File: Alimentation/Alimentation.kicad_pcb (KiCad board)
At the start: 2 copper layers, 63.5 x 108 mm, 18 parts, among them J1 connector_battery, J2 connector_battery, J3 RJ_can, J4 USB_A, J5 Conn_01x02_Male, J6 Conn_01x03_Male, J7 Conn_01x02_Male, U1 JCK2012S12, U2 JCK2012S05

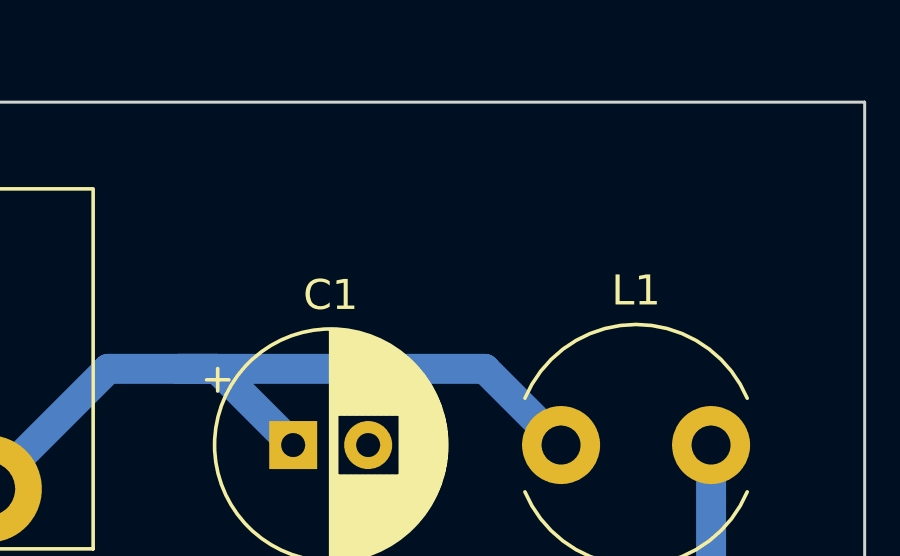
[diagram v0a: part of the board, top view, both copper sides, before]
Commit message: Ajout de la led
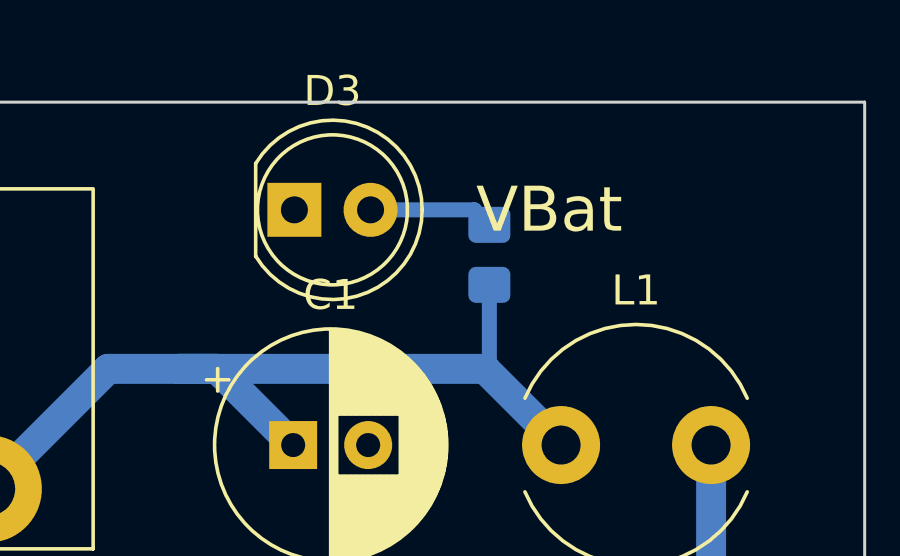
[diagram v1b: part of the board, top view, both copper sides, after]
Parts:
- added D3: LED, LED_THT:LED_D5.0mm, F.Cu at (124.5, 45.5)
- added R4: 1500, Resistor_SMD:R_0805_2012Metric_Pad1.20x1.40mm_HandSolder, B.Cu at (131.0, 47.0)
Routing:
- net Net-(D3-Pad2): track 0.00 -> 4.17 mm
- net V_batt: track 58.4 -> 61.3 mm
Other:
- board text added: "VBat"
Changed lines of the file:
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@@
   (net 15 "unconnected-(U2-Pad4)")
   (net 16 "unconnected-(U2-Pad6)")
+  (net 17 "Net-(D3-Pad2)")
   (footprint "Inductor_THT:L_Radial_D7.8mm_P5.00mm_Fastron_07HCP" (layer "F.Cu")
     (at 133.39 53.34)
@@
     )
   )
+  (footprint "LED_THT:LED_D5.0mm" (layer "F.Cu")
+    (at 124.5 45.5)
+    (descr "LED, diameter 5.0mm, 2 pins, http://cdn-reichelt.de/documents/datenblatt/A500/LL-504BC2E-009.pdf")
+    (tags "LED diameter 5.0mm 2 pins")
+    (property "Sheetfile" "Alimentation.kicad_sch")
+    (property "Sheetname" "")
+    (attr through_hole)
+    (fp_text reference "D3" (at 1.27 -3.96) (layer "F.SilkS")
+      (effects (font (size 1 1) (thickness 0.15)))
+    )
+    (fp_text value "LED" (at 1.27 3.96) (layer "F.Fab")
+      (effects (font (size 1 1) (thickness 0.15)))
+    )
+    (fp_text user "${REFERENCE}" (at 1.25 0) (layer "F.Fab")
+      (effects (font (size 0.8 0.8) (thickness 0.2)))
+    )
+    (fp_line (start -1.29 -1.545) (end -1.29 1.545) (layer "F.SilkS") (width 0.12))
+    (fp_arc (start 4.26 -0.000462) (mid 2.072002 2.880433) (end -1.29 1.54483) (layer "F.SilkS") (width 0.12))
+    (fp_arc (start -1.29 -1.54483) (mid 2.072002 -2.880433) (end 4.26 0.000462) (layer "F.SilkS") (width 0.12))
+    (fp_circle (center 1.27 0) (end 3.77 0) (layer "F.SilkS") (width 0.12) (fill none))
+    (fp_line (start -1.95 3.25) (end 4.5 3.25) (layer "F.CrtYd") (width 0.05))
+    (fp_line (start 4.5 3.25) (end 4.5 -3.25) (layer "F.CrtYd") (width 0.05))
+    (fp_line (start -1.95 -3.25) (end -1.95 3.25) (layer "F.CrtYd") (width 0.05))
+    (fp_line (start 4.5 -3.25) (end -1.95 -3.25) (layer "F.CrtYd") (width 0.05))
+    (fp_line (start -1.23 -1.469694) (end -1.23 1.469694) (layer "F.Fab") (width 0.1))
+    (fp_arc (start -1.23 -1.469694) (mid 4.17 0.000016) (end -1.230016 1.469666) (layer "F.Fab") (width 0.1))
+    (fp_circle (center 1.27 0) (end 3.77 0) (layer "F.Fab") (width 0.1) (fill none))
+    (pad "1" thru_hole rect (at 0 0) (size 1.8 1.8) (drill 0.9) (layers *.Cu *.Mask)
+      (net 2 "GND") (pinfunction "K") (pintype "passive"))
+    (pad "2" thru_hole circle (at 2.54 0) (size 1.8 1.8) (drill 0.9) (layers *.Cu *.Mask)
+      (net 17 "Net-(D3-Pad2)") (pinfunction "A") (pintype "passive"))
+    (model "${KICAD6_3DMODEL_DIR}/LED_THT.3dshapes/LED_D5.0mm.wrl"
+      (offset (xyz 0 0 0))
+      (scale (xyz 1 1 1))
+      (rotate (xyz 0 0 0))
+    )
+  )
   (footprint "Connector_PinHeader_2.54mm:PinHeader_1x03_P2.54mm_Horizontal" (layer "F.Cu")
     (at 92.71 129.525 180)
@@
     )
   )
+  (footprint "Resistor_SMD:R_0805_2012Metric_Pad1.20x1.40mm_HandSolder" (layer "B.Cu")
+    (at 131 47 90)
+    (descr "Resistor SMD 0805 (2012 Metric), square (rectangular) end terminal, IPC_7351 nominal with elongated pad for handsoldering. (Body size source: IPC-SM-782 page 72, https://www.pcb-3d.com/wordpress/wp-content/uploads/ipc-sm-782a_amendment_1_and_2.pdf), generated with kicad-footprint-generator")
+    (tags "resistor handsolder")
+    (property "Sheetfile" "Alimentation.kicad_sch")
+    (property "Sheetname" "")
+    (attr smd)
+    (fp_text reference "R4" (at 0 1.65 90) (layer "B.SilkS")
+      (effects (font (size 1 1) (thickness 0.15)) (justify mirror))
+    )
+    (fp_text value "1500" (at 0 -1.65 90) (layer "B.Fab")
+      (effects (font (size 1 1) (thickness 0.15)) (justify mirror))
+    )
+    (fp_text user "${REFERENCE}" (at 0 0 90) (layer "B.Fab")
+      (effects (font (size 0.5 0.5) (thickness 0.08)) (justify mirror))
+    )
+    (fp_line (start -0.227064 -0.735) (end 0.227064 -0.735) (layer "B.SilkS") (width 0.12))
+    (fp_line (start -0.227064 0.735) (end 0.227064 0.735) (layer "B.SilkS") (width 0.12))
+    (fp_line (start 1.85 -0.95) (end -1.85 -0.95) (layer "B.CrtYd") (width 0.05))
+    (fp_line (start 1.85 0.95) (end 1.85 -0.95) (layer "B.CrtYd") (width 0.05))
+    (fp_line (start -1.85 -0.95) (end -1.85 0.95) (layer "B.CrtYd") (width 0.05))
+    (fp_line (start -1.85 0.95) (end 1.85 0.95) (layer "B.CrtYd") (width 0.05))
+    (fp_line (start 1 -0.625) (end -1 -0.625) (layer "B.Fab") (width 0.1))
+    (fp_line (start -1 -0.625) (end -1 0.625) (layer "B.Fab") (width 0.1))
+    (fp_line (start 1 0.625) (end 1 -0.625) (layer "B.Fab") (width 0.1))
+    (fp_line (start -1 0.625) (end 1 0.625) (layer "B.Fab") (width 0.1))
+    (pad "1" smd roundrect (at -1 0 90) (size 1.2 1.4) (layers "B.Cu" "B.Paste" "B.Mask") (roundrect_rratio 0.208333)
+      (net 1 "V_batt") (pintype "passive"))
+    (pad "2" smd roundrect (at 1 0 90) (size 1.2 1.4) (layers "B.Cu" "B.Paste" "B.Mask") (roundrect_rratio 0.208333)
+      (net 17 "Net-(D3-Pad2)") (pintype "passive"))
+    (model "${KICAD6_3DMODEL_DIR}/Resistor_SMD.3dshapes/R_0805_2012Metric.wrl"
+      (offset (xyz 0 0 0))
+      (scale (xyz 1 1 1))
+      (rotate (xyz 0 0 0))
+    )
+  )
   (gr_rect (start 80.01 41.91) (end 143.51 149.86) (layer "Edge.Cuts") (width 0.1) (fill none))
   (gr_text "JCK2012S05" (at 96.52 86.36) (layer "F.SilkS")
@@
     (effects (font (size 1 1) (thickness 0.15)))
   )
+  (gr_text "VBat" (at 133 45.5) (layer "F.SilkS")
+    (effects (font (size 1.5 1.5) (thickness 0.3)))
+  )
   (gr_text "GND" (at 83.82 123.19) (layer "F.SilkS")
     (effects (font (size 1 1) (thickness 0.15)))
@@
   (segment (start 99.06 53.34) (end 101.6 50.8) (width 1) (layer "B.Cu") (net 1))
   (segment (start 114.2925 54.8) (end 118.2925 50.8) (width 1) (layer "B.Cu") (net 1))
+  (segment (start 131 50.65) (end 130.85 50.8) (width 0.5) (layer "B.Cu") (net 1))
   (segment (start 102.87 50.8) (end 92.67 50.8) (width 1) (layer "B.Cu") (net 1))
+  (segment (start 131 48) (end 131 50.65) (width 0.5) (layer "B.Cu") (net 1))
   (segment (start 110.2925 50.8) (end 102.87 50.8) (width 1) (layer "B.Cu") (net 1))
   (segment (start 120.65 50.8) (end 130.85 50.8) (width 1) (layer "B.Cu") (net 1))
@@
   (segment (start 85.13 53.34) (end 85.13 66.745) (width 1) (layer "B.Cu") (net 12))
   (segment (start 85.13 66.745) (end 93.98 75.595) (width 1) (layer "B.Cu") (net 12))
+  (segment (start 127.04 45.5) (end 130.5 45.5) (width 0.5) (layer "B.Cu") (net 17))
+  (segment (start 130.5 45.5) (end 131 46) (width 0.5) (layer "B.Cu") (net 17))
   (zone (net 2) (net_name "GND") (layer "B.Cu") (hatch edge 0.508)
     (connect_pads (clearance 0.508))

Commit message: Update alimentation; Add Base roulante
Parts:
- J2: value connector_battery -> connector_power
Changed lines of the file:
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@@
       (effects (font (size 1 1) (thickness 0.15)))
     )
-    (fp_text value "connector_battery" (at 0 0 unlocked) (layer "F.Fab")
+    (fp_text value "connector_power" (at 0 0 unlocked) (layer "F.Fab")
       (effects (font (size 1 1) (thickness 0.15)))
     )

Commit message: Commande
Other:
- board text added: "AAA Louis Chauvet"
- board text added: "JLCJLCJLCJLC"
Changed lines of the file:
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@@
   )
   (paper "A4")
+  (title_block
+    (title "Alimentation principale")
+    (date "2022-07-25")
+    (rev "V1")
+    (company "Club robot")
+    (comment 1 "Louis Chauvet")
+  )
   (layers
     (0 "F.Cu" signal)
@@
       (layerselection 0x00010fc_ffffffff)
       (disableapertmacros false)
-      (usegerberextensions false)
-      (usegerberattributes true)
-      (usegerberadvancedattributes true)
-      (creategerberjobfile true)
+      (usegerberextensions true)
+      (usegerberattributes false)
+      (usegerberadvancedattributes false)
+      (creategerberjobfile false)
       (svguseinch false)
       (svgprecision 6)
@@
       (psa4output false)
       (plotreference true)
-      (plotvalue true)
+      (plotvalue false)
       (plotinvisibletext false)
       (sketchpadsonfab false)
-      (subtractmaskfromsilk false)
+      (subtractmaskfromsilk true)
       (outputformat 1)
       (mirror false)
-      (drillshape 1)
+      (drillshape 0)
       (scaleselection 1)
       (outputdirectory "")
@@
     (property "Sheetname" "")
     (attr through_hole)
-    (fp_text reference "C1" (at 1.25 -5) (layer "F.SilkS")
+    (fp_text reference "C1" (at 1.25 5.08) (layer "F.SilkS")
       (effects (font (size 1 1) (thickness 0.15)))
     )
@@
     (property "Sheetname" "")
     (attr through_hole)
-    (fp_text reference "D3" (at 1.27 -3.96) (layer "F.SilkS")
+    (fp_text reference "D3" (at -3.85 0.22) (layer "F.SilkS") hide
       (effects (font (size 1 1) (thickness 0.15)))
     )
@@
     (fp_line (start -1 -0.625) (end -1 0.625) (layer "B.Fab") (width 0.1))
     (fp_line (start 1 0.625) (end 1 -0.625) (layer "B.Fab") (width 0.1))
-    (pad "1" smd roundrect (at -1 0 90) (size 1.2 1.4) (layers "B.Cu" "B.Paste" "B.Mask") (roundrect_rratio 0.208333)
+    (pad "1" smd roundrect (at -1 0 90) (size 1.2 1.4) (layers "B.Cu" "B.Paste" "B.Mask") (roundrect_rratio 0.2083333333)
       (net 7 "CAN_H") (pintype "passive"))
-    (pad "2" smd roundrect (at 1 0 90) (size 1.2 1.4) (layers "B.Cu" "B.Paste" "B.Mask") (roundrect_rratio 0.208333)
+    (pad "2" smd roundrect (at 1 0 90) (size 1.2 1.4) (layers "B.Cu" "B.Paste" "B.Mask") (roundrect_rratio 0.2083333333)
       (net 6 "CAN_L") (pintype "passive"))
     (model "${KICAD6_3DMODEL_DIR}/Resistor_SMD.3dshapes/R_0805_2012Metric.wrl"
@@
     (fp_line (start 1 0.625) (end 1 -0.625) (layer "B.Fab") (width 0.1))
     (fp_line (start 1 -0.625) (end -1 -0.625) (layer "B.Fab") (width 0.1))
-    (pad "1" smd roundrect (at -1 0 270) (size 1.2 1.4) (layers "B.Cu" "B.Paste" "B.Mask") (roundrect_rratio 0.208333)
+    (pad "1" smd roundrect (at -1 0 270) (size 1.2 1.4) (layers "B.Cu" "B.Paste" "B.Mask") (roundrect_rratio 0.2083333333)
       (net 5 "+12V") (pintype "passive"))
-    (pad "2" smd roundrect (at 1 0 270) (size 1.2 1.4) (layers "B.Cu" "B.Paste" "B.Mask") (roundrect_rratio 0.208333)
+    (pad "2" smd roundrect (at 1 0 270) (size 1.2 1.4) (layers "B.Cu" "B.Paste" "B.Mask") (roundrect_rratio 0.2083333333)
       (net 4 "Net-(D2-Pad2)") (pintype "passive"))
     (model "${KICAD6_3DMODEL_DIR}/Resistor_SMD.3dshapes/R_0805_2012Metric.wrl"
@@
     (fp_line (start -1 0.625) (end 1 0.625) (layer "B.Fab") (width 0.1))
     (fp_line (start -1 -0.625) (end -1 0.625) (layer "B.Fab") (width 0.1))
-    (pad "1" smd roundrect (at -1 0 270) (size 1.2 1.4) (layers "B.Cu" "B.Paste" "B.Mask") (roundrect_rratio 0.208333)
+    (pad "1" smd roundrect (at -1 0 270) (size 1.2 1.4) (layers "B.Cu" "B.Paste" "B.Mask") (roundrect_rratio 0.2083333333)
       (net 8 "+5V") (pintype "passive"))
-    (pad "2" smd roundrect (at 1 0 270) (size 1.2 1.4) (layers "B.Cu" "B.Paste" "B.Mask") (roundrect_rratio 0.208333)
+    (pad "2" smd roundrect (at 1 0 270) (size 1.2 1.4) (layers "B.Cu" "B.Paste" "B.Mask") (roundrect_rratio 0.2083333333)
       (net 3 "Net-(D1-Pad2)") (pintype "passive"))
     (model "${KICAD6_3DMODEL_DIR}/Resistor_SMD.3dshapes/R_0805_2012Metric.wrl"
@@
     (fp_line (start 1 0.625) (end 1 -0.625) (layer "B.Fab") (width 0.1))
     (fp_line (start -1 0.625) (end 1 0.625) (layer "B.Fab") (width 0.1))
-    (pad "1" smd roundrect (at -1 0 90) (size 1.2 1.4) (layers "B.Cu" "B.Paste" "B.Mask") (roundrect_rratio 0.208333)
+    (pad "1" smd roundrect (at -1 0 90) (size 1.2 1.4) (layers "B.Cu" "B.Paste" "B.Mask") (roundrect_rratio 0.2083333333)
       (net 1 "V_batt") (pintype "passive"))
-    (pad "2" smd roundrect (at 1 0 90) (size 1.2 1.4) (layers "B.Cu" "B.Paste" "B.Mask") (roundrect_rratio 0.208333)
+    (pad "2" smd roundrect (at 1 0 90) (size 1.2 1.4) (layers "B.Cu" "B.Paste" "B.Mask") (roundrect_rratio 0.2083333333)
       (net 17 "Net-(D3-Pad2)") (pintype "passive"))
     (model "${KICAD6_3DMODEL_DIR}/Resistor_SMD.3dshapes/R_0805_2012Metric.wrl"
@@
     (effects (font (size 1 1) (thickness 0.15)))
   )
+  (gr_text "AAA\nLouis Chauvet" (at 86.995 139.7) (layer "F.SilkS")
+    (effects (font (size 1 1) (thickness 0.15)))
+  )
   (gr_text "+12V" (at 140.97 114.3) (layer "F.SilkS")
     (effects (font (size 1 1) (thickness 0.15)))
@@
     (effects (font (size 1 1) (thickness 0.15)))
   )
+  (gr_text "JLCJLCJLCJLC" (at 101.6 108.585) (layer "F.SilkS")
+    (effects (font (size 1 1) (thickness 0.15)))
+  )

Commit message: Update card to cut board near to the connector
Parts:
- moved D3 18.4 mm to (139.7, 55.9), turned to 90 degrees
- moved R4 7.85 mm to (138.4, 49.5), turned to 0 degrees
- moved L1 3.85 mm to (129.5, 53.3)
- moved L2 3.81 mm to (93.9, 53.3)
- moved C1 2.54 mm to (121.9, 53.3)
- moved C2 2.54 mm to (101.6, 53.3)
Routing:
- net V_batt: track 61.3 -> 57.9 mm
- net Net-(L1-Pad2): track 28.0 -> 26.4 mm
- net Net-(L2-Pad2): track 25.9 -> 24.3 mm
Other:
- board size 63.5 x 108 mm -> 63.5 x 99.1 mm
- board text added: "REFREFREF Louis Chauvet Andrea Perez"
- board text removed: "AAA Louis Chauvet"
